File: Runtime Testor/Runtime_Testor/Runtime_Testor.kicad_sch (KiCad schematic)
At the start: 37 parts, among them CON1 SWD, J1 ESP8266, J2 USB_A, SW1 SW_SPDT, SW2 SW_Push, U1 FRAM, U2 AMS1117-3.3, U3 STM32F103C8T6, Y1 16MHz

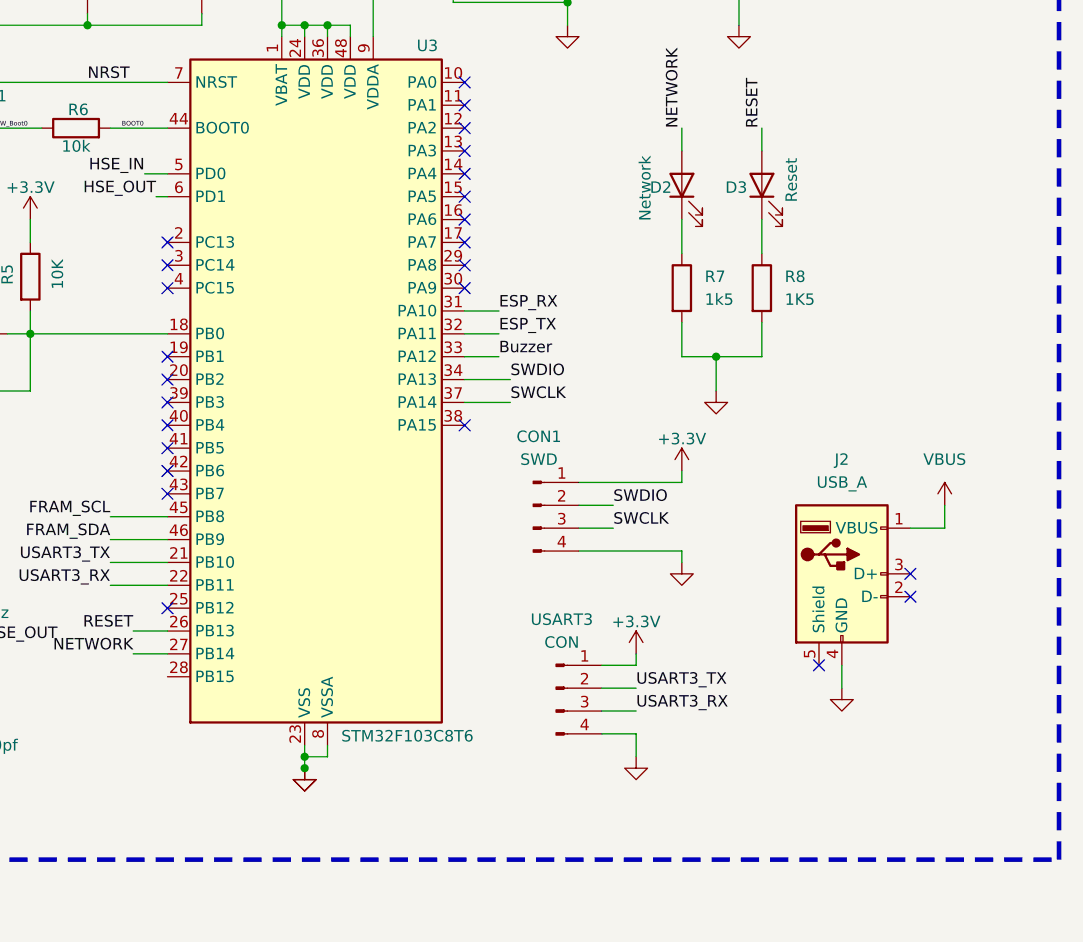
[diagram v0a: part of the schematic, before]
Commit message: Added USB Port for UART communication
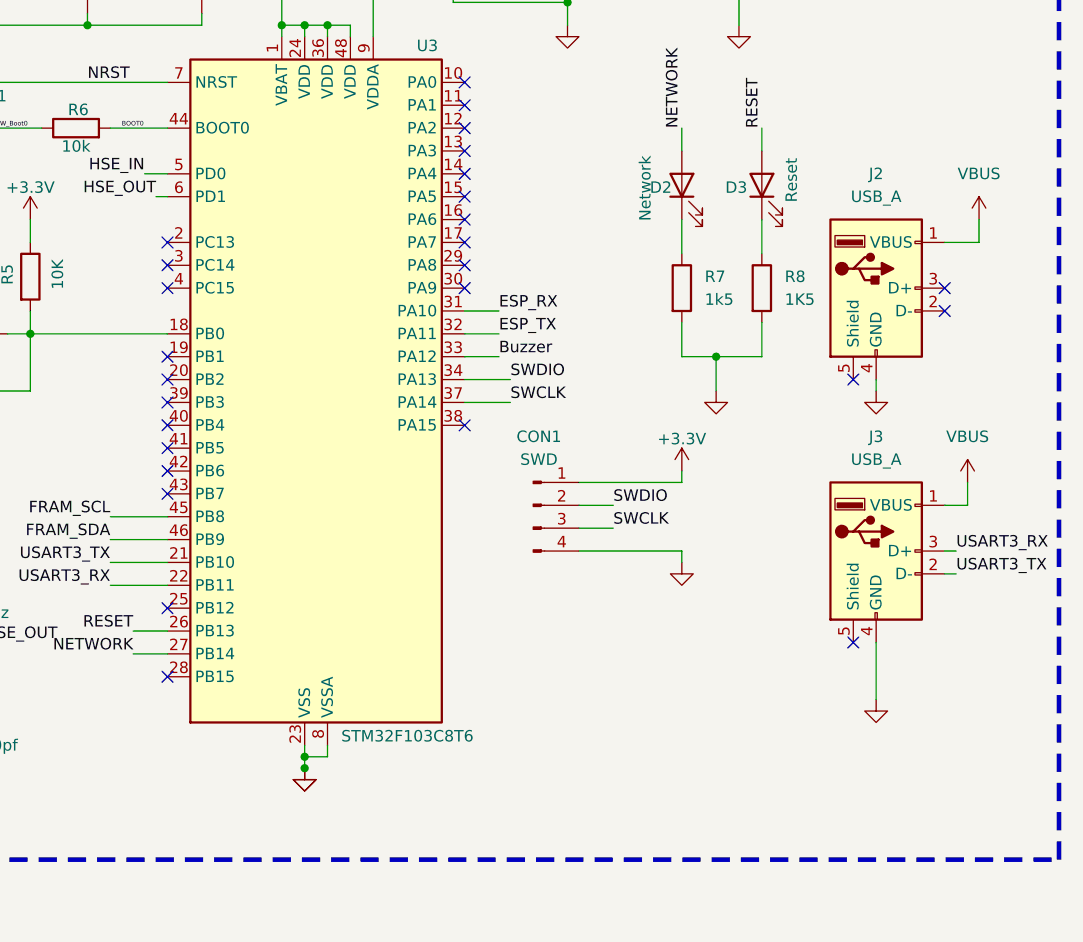
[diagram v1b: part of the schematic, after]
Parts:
- removed USART3: CON, Connector_PinHeader_2.54mm:PinHeader_1x04_P2.54mm_Vertical, symbol Connector:Conn_01x04_Pin
- added J3: USB_A, Connector_USB:USB_A_Molex_67643_Horizontal, symbol Connector:USB_A
- SW1: footprint Button_Switch_THT:SW_Slide_SPDT_Straight_CK_OS102011MS2Q -> Button_Switch_THT:SW_Slide_SPDT_Angled_CK_OS102011MA1Q
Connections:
- net GND: now also J3.4 (GND)
- net USART3_RX: now also J3.3 (D+)
- net USART3_TX: now also J3.2 (D-)
- net VBUS: now also J3.1 (VBUS)
- no-connect marks 33 -> 35
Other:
- moved on the sheet: J2
